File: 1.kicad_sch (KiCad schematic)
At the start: 1 part, among them U1 EPM240T100

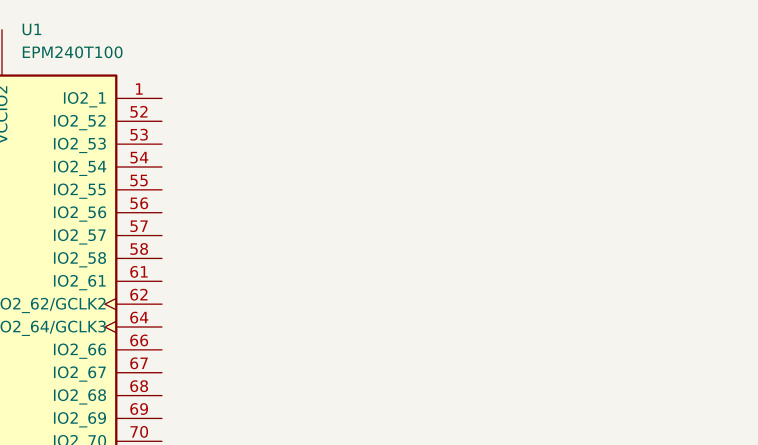
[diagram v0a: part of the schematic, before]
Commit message: open with 10
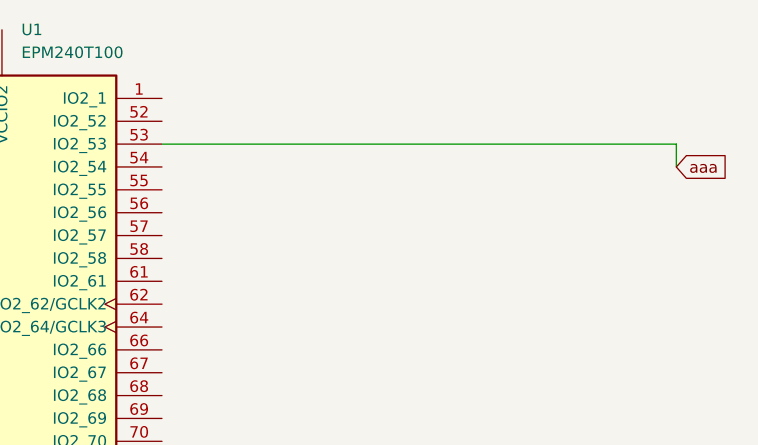
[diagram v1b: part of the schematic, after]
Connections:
- net aaa: now reaches U1.53 (IO2_53)
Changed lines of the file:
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@@
 (kicad_sch
-	(version 20250114)
+	(version 20260101)
 	(generator "eeschema")
-	(generator_version "9.0")
+	(generator_version "10.0")
 	(paper "A4")
+	(wire
+		(pts
+			(xy 181.61 57.15) (xy 181.61 59.69)
+		)
+		(stroke
+			(width 0)
+			(type default)
+		)
+	)
+	(wire
+		(pts
+			(xy 124.46 57.15) (xy 181.61 57.15)
+		)
+		(stroke
+			(width 0)
+			(type default)
+		)
+	)
+	(global_label "aaa"
+		(shape input)
+		(at 181.61 59.69 0)
+		(fields_autoplaced yes)
+		(effects
+			(font
+				(size 1.27 1.27)
+			)
+			(justify left)
+		)
+		(property "Intersheetrefs" "${INTERSHEET_REFS}"
+			(at 188.0422 59.69 0)
+			(hide yes)
+			(show_name no)
+			(do_not_autoplace no)
+			(effects
+				(font
+					(size 1.27 1.27)
+				)
+				(justify left)
+			)
+		)
+	)
 	(symbol
 		(lib_id "CPLD_Altera:EPM240T100")
 		(at 99.06 105.41 0)
 		(unit 1)
+		(body_style 1)
 		(exclude_from_sim no)
 		(in_bom yes)
 		(on_board yes)
+		(in_pos_files yes)
 		(dnp no)
 		(fields_autoplaced yes)
 		(property "Reference" "U1"
 			(at 108.8233 44.45 0)
+			(show_name no)
+			(do_not_autoplace no)
 			(effects
 				(font
@@
 		(property "Value" "EPM240T100"
 			(at 108.8233 46.99 0)
+			(show_name no)
+			(do_not_autoplace no)
 			(effects
 				(font
@@
 		(property "Footprint" "Package_QFP:LQFP-100_14x14mm_P0.5mm"
 			(at 109.22 165.1 0)
+			(hide yes)
+			(show_name no)
+			(do_not_autoplace no)
 			(effects
 				(font
@@
 				)
 				(justify left)
-				(hide yes)
 			)
 		)
 		(property "Datasheet" "https://www.altera.com/content/dam/altera-www/global/en_US/pdfs/literature/hb/max2/max2_mii5v1.pdf"
 			(at 99.06 105.41 0)
+			(hide yes)
+			(show_name no)
+			(do_not_autoplace no)
 			(effects
 				(font
 					(size 1.27 1.27)
 				)
-				(hide yes)
 			)
 		)
 		(property "Description" "Altera MAX2 CPLD with 240 LE"
 			(at 99.06 105.41 0)
+			(hide yes)
+			(show_name no)
+			(do_not_autoplace no)
 			(effects
 				(font
 					(size 1.27 1.27)
 				)
-				(hide yes)
 			)
 		)
